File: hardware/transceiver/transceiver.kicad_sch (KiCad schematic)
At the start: 36 parts, among them J1 Conn_01x02, J2 Conn_01x04, J3 Micro_SD_Card_Det_Hirose_DM3AT, J4 Conn_Coaxial_Small, SW1 Reset, SW2 Boot, U1 SX1262IMLTRT, U2 PE4259, U4 ESP32-S3-MINI-1, Y1 32MHz

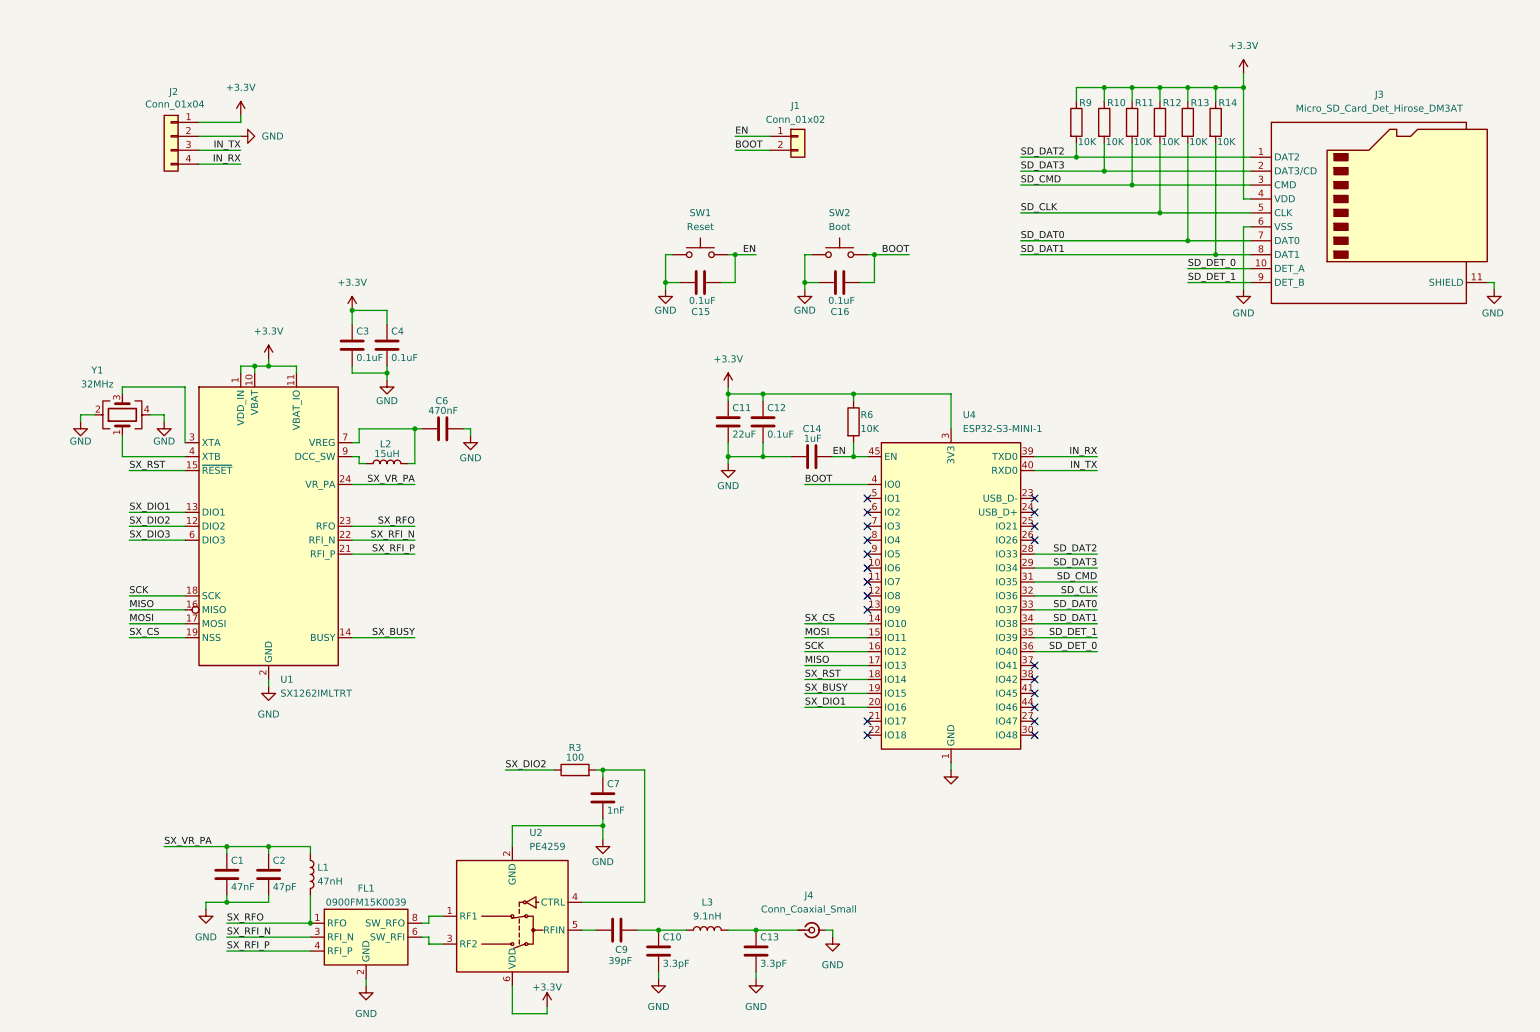
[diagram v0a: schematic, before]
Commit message: redesigned tranceiver
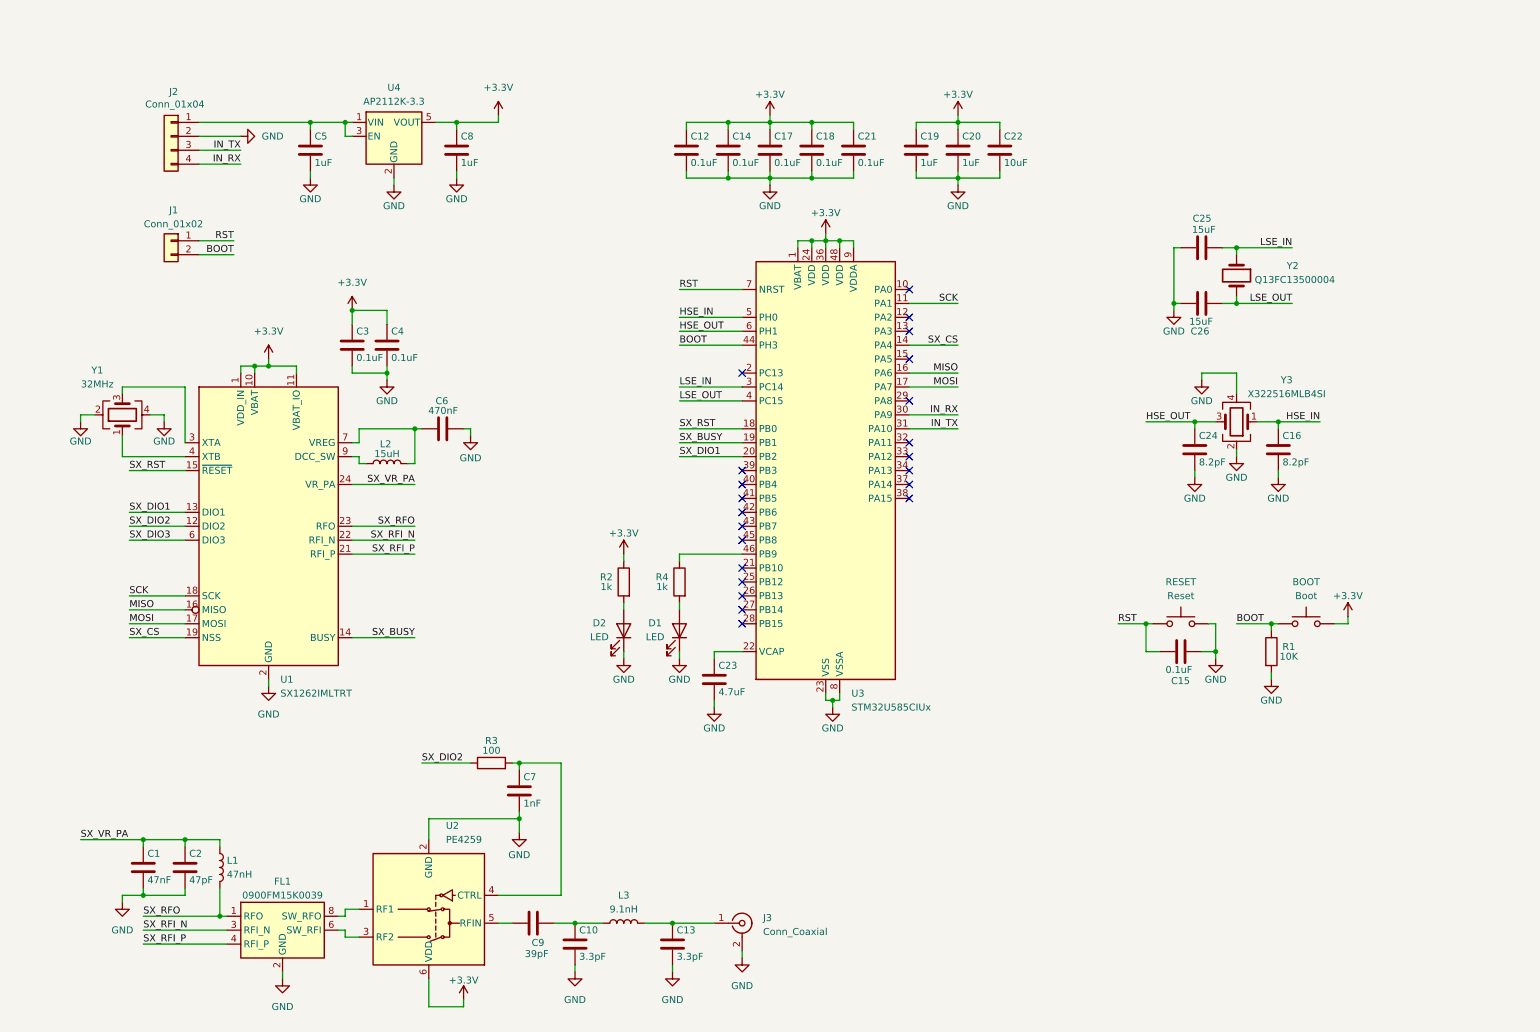
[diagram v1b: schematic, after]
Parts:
- removed C11: 22uF, Capacitor_SMD:C_0603_1608Metric, symbol Device:C
- removed J3: Micro_SD_Card_Det_Hirose_DM3AT, Connector_Card:microSD_HC_Hirose_DM3AT-SF-PEJM5, symbol Connector:Micro_SD_Card_Det_Hirose_DM3AT
- removed J4: Conn_Coaxial_Small, Connector_Coaxial:U.FL_Molex_MCRF_73412-0110_Vertical, symbol Connector:Conn_Coaxial_Small
- removed R10, R11, R12, R13, R14, R6, R9: 10K, Resistor_SMD:R_0402_1005Metric, symbol Device:R
- removed SW2: Boot, Button_Switch_SMD:SW_Push_SPST_NO_Alps_SKRK, symbol Switch:SW_Push
- removed U4: ESP32-S3-MINI-1, RF_Module:ESP32-S2-MINI-1, symbol RF_Module:ESP32-S3-MINI-1
- added BOOT: Boot, Button_Switch_SMD:SW_Push_SPST_NO_Alps_SKRK, symbol Switch:SW_Push
- added C17, C18, C21: 0.1uF, Capacitor_SMD:C_0402_1005Metric, symbol Device:C
- added C19, C20, C5, C8: 1uF, Capacitor_SMD:C_0603_1608Metric, symbol Device:C
- added C22: 10uF, Capacitor_SMD:C_0603_1608Metric, symbol Device:C
- added C23: 4.7uF, Capacitor_SMD:C_0402_1005Metric, symbol Device:C
- added C24: 8.2pF, Capacitor_SMD:C_0402_1005Metric, symbol Device:C
- added C25, C26: 15uF, Capacitor_SMD:C_0402_1005Metric, symbol Device:C
- added D1, D2: LED, LED_SMD:LED_0603_1608Metric, symbol Device:LED
- added J3: Conn_Coaxial, Connector_Coaxial:SMA_Amphenol_901-144_Vertical, symbol Connector:Conn_Coaxial
- added R1: 10K, Resistor_SMD:R_0402_1005Metric, symbol Device:R
- added R2, R4: 1k, Resistor_SMD:R_0402_1005Metric, symbol Device:R
- added U3: STM32U585CIUx, Package_DFN_QFN:QFN-48-1EP_7x7mm_P0.5mm_EP5.6x5.6mm, symbol MCU_ST_STM32U5:STM32U585CIUx
- added U4: AP2112K-3.3, Package_TO_SOT_SMD:SOT-23-5, symbol Regulator_Linear:AP2112K-3.3
- added Y2: Q13FC13500004, Crystal:Crystal_SMD_3215-2Pin_3.2x1.5mm, symbol Device:Crystal
- added Y3: X322516MLB4SI, Crystal:Crystal_SMD_3225-4Pin_3.2x2.5mm, symbol Device:Crystal_GND24
- C14: value 1uF -> 0.1uF
- C16: value 0.1uF -> 8.2pF
- renumbered SW1 to RESET
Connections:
- net +3.3V: now also C14.1, BOOT.1, C17.1, C18.1, C19.1, C20.1, C21.1, C22.1, C8.1, R2.1, U3.1 (VBAT), U3.24 (VDD), U3.36 (VDD), U3.48 (VDD), U3.9 (VDDA), U4.5 (VOUT); no longer J2.1 (Pin_1)
- net BOOT: now also BOOT.2, R1.1, U3.44 (PH3); no longer C16.2
- net GND: now also C14.2, C16.2, C17.2, C18.2, C19.2, C20.2, C21.2, C22.2, C23.2, C24.2, C25.1, C26.2, C5.2, C8.2, D1.1 (K), D2.1 (K), J3.2 (Ext), R1.2, U3.23 (VSS), U3.35 (VSS), U3.47 (VSS), U3.49 (VSS), U3.8 (VSSA), U4.2 (GND), Y3.2, Y3.4; no longer C14.1, C16.1
- net IN_RX: now also U3.30 (PA9)
- net IN_TX: now also U3.31 (PA10)
- net MISO: now also U3.16 (PA6)
- net MOSI: now also U3.17 (PA7)
- net SCK: now also U3.11 (PA1)
- net SX_BUSY: now also U3.19 (PB1)
- net SX_CS: now also U3.14 (PA4)
- net SX_DIO1: now also U3.20 (PB2)
- net SX_RST: now also U3.18 (PB0)
- net at C13.1, L3.2: now also J3.1 (In)
- net EN renamed RST
- net RST: now also U3.7 (NRST); no longer C14.2
- new net: C5.1, J2.1 (Pin_1), U4.1 (VIN), U4.3 (EN)
- new net: D2.2 (A), R2.2
- new net: D1.2 (A), R4.2
- new net: C23.1, U3.22 (VCAP)
- new net: R4.1, U3.46 (PB9)
- new net HSE_IN: C16.1, U3.5 (PH0), Y3.1
- new net HSE_OUT: C24.1, U3.6 (PH1), Y3.3
- new net LSE_IN: C25.2, U3.3 (PC14), Y2.1
- new net LSE_OUT: C26.1, U3.4 (PC15), Y2.2
- no-connect marks 21 -> 22
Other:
- moved on the sheet: C1, C10, C13, C15, C2, C7, C9, FL1, J1, L1, L3, R3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

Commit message: cleaning up transceiver
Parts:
- renumbered BOOT to BOOT1, C13 to C11, C23 to C13, C17 to C15, C18 to C16, C21 to C17, C19 to C18, C20 to C19, C22 to C20, C15 to C21, C24 to C22, C25 to C23, C26 to C24, C16 to C25, C5 to C3, C3 to C4, C4 to C5, C8 to C7, C7 to C8, D2 to D1, D1 to D2, J2 to J1, J1 to J2, R3 to R1, R4 to R3, R1 to R4, RESET to RESET1, U4 to U2, U2 to U3, U3 to U4

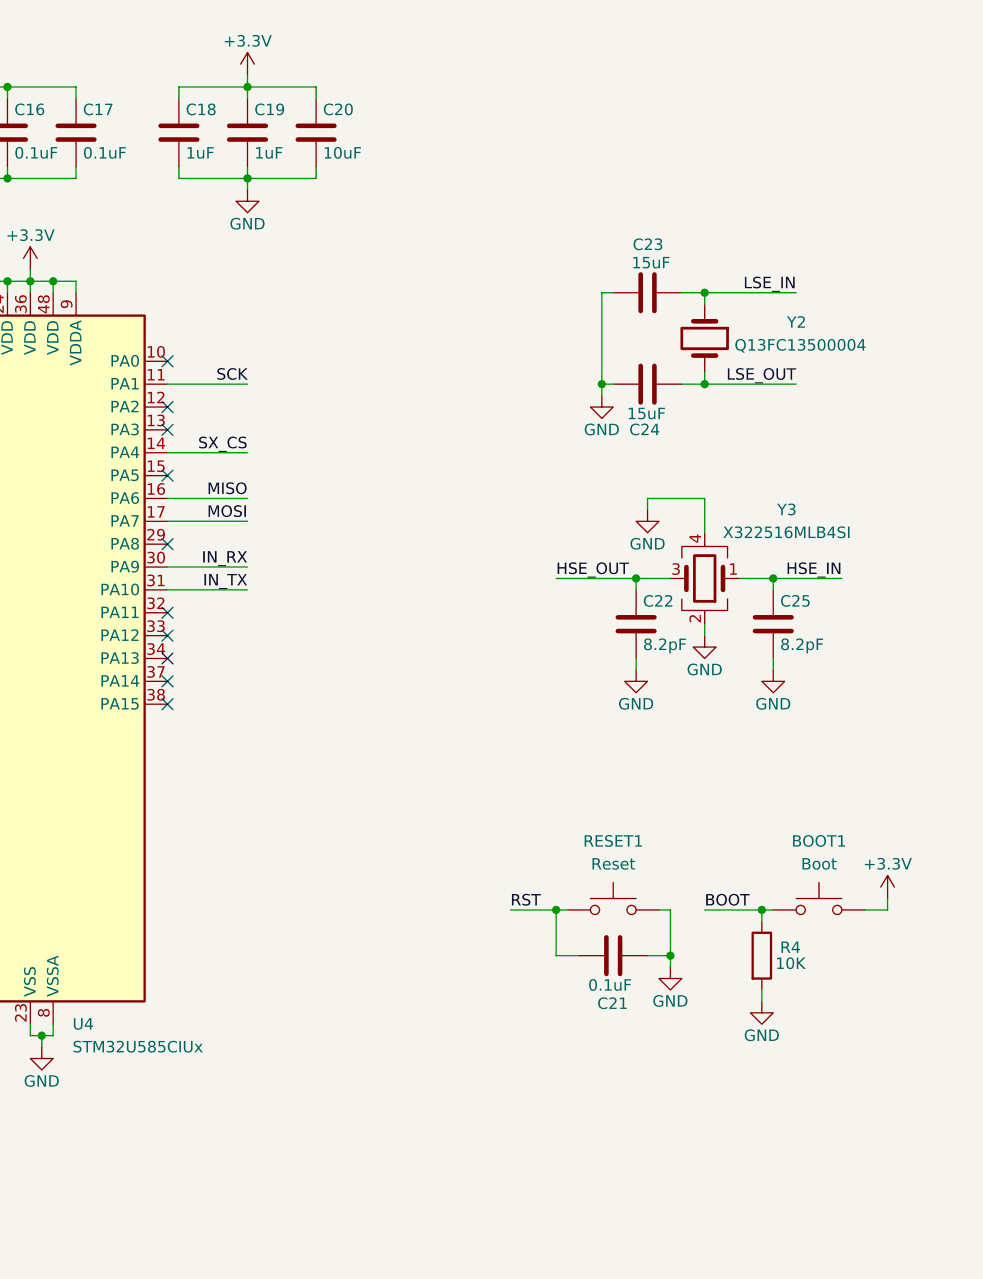
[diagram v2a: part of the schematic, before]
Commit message: added SWD to transceiver
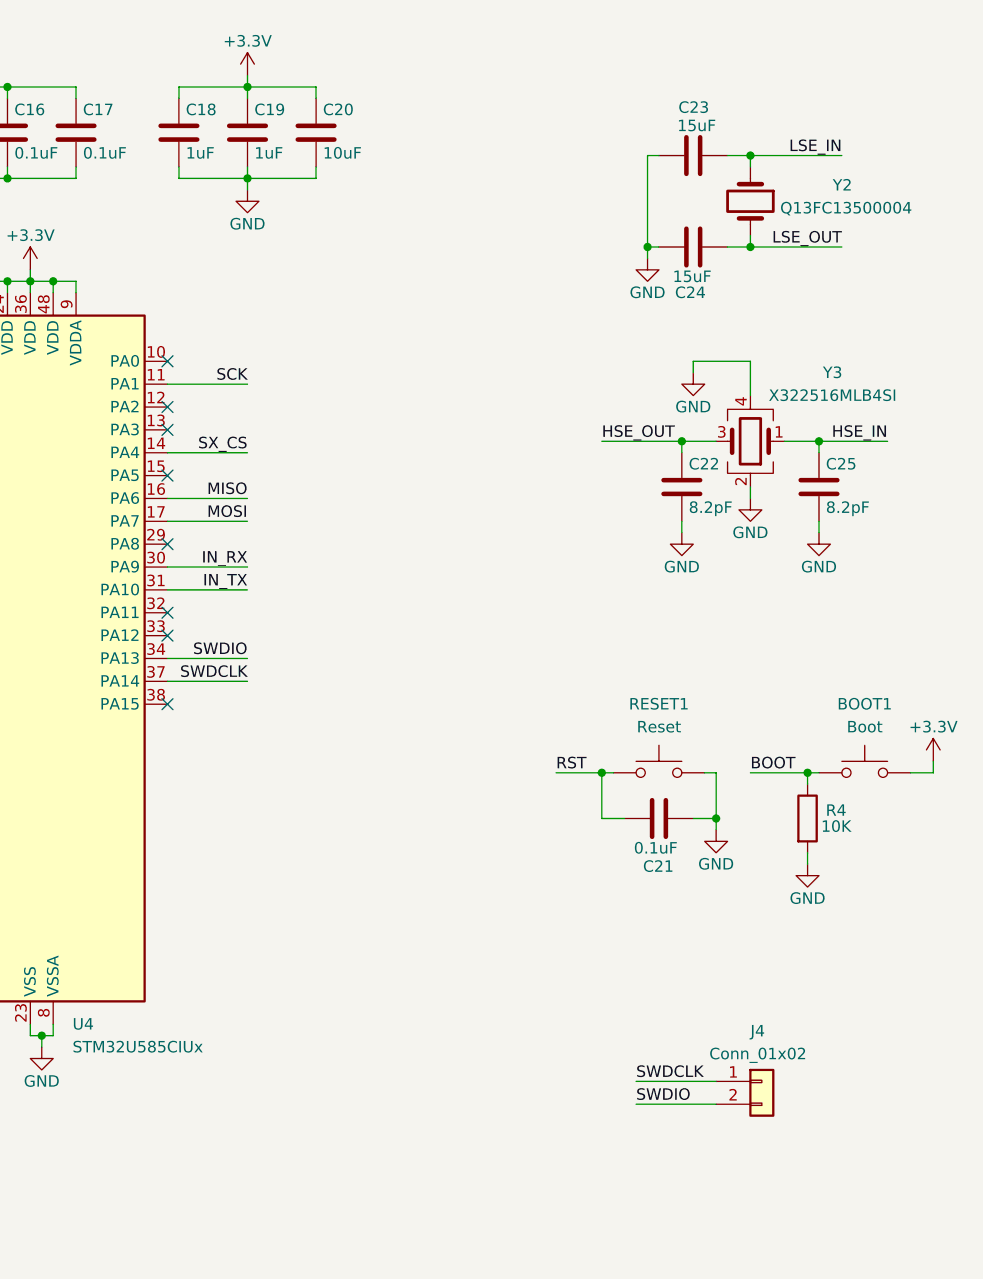
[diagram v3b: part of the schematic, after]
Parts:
- added J4: Conn_01x02, Connector_PinHeader_2.54mm:PinHeader_1x02_P2.54mm_Vertical, symbol Connector_Generic:Conn_01x02
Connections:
- net SWDIO: now reaches U4.34 (PA13)
- net SWDIO: now also J4.2 (Pin_2)
- net SWDCLK: now reaches U4.37 (PA14)
- net SWDCLK: now also J4.1 (Pin_1)
- no-connect marks 22 -> 20
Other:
- moved on the sheet: BOOT1, C21, C22, C23, C24, C25, R4, RESET1, Y2, Y3

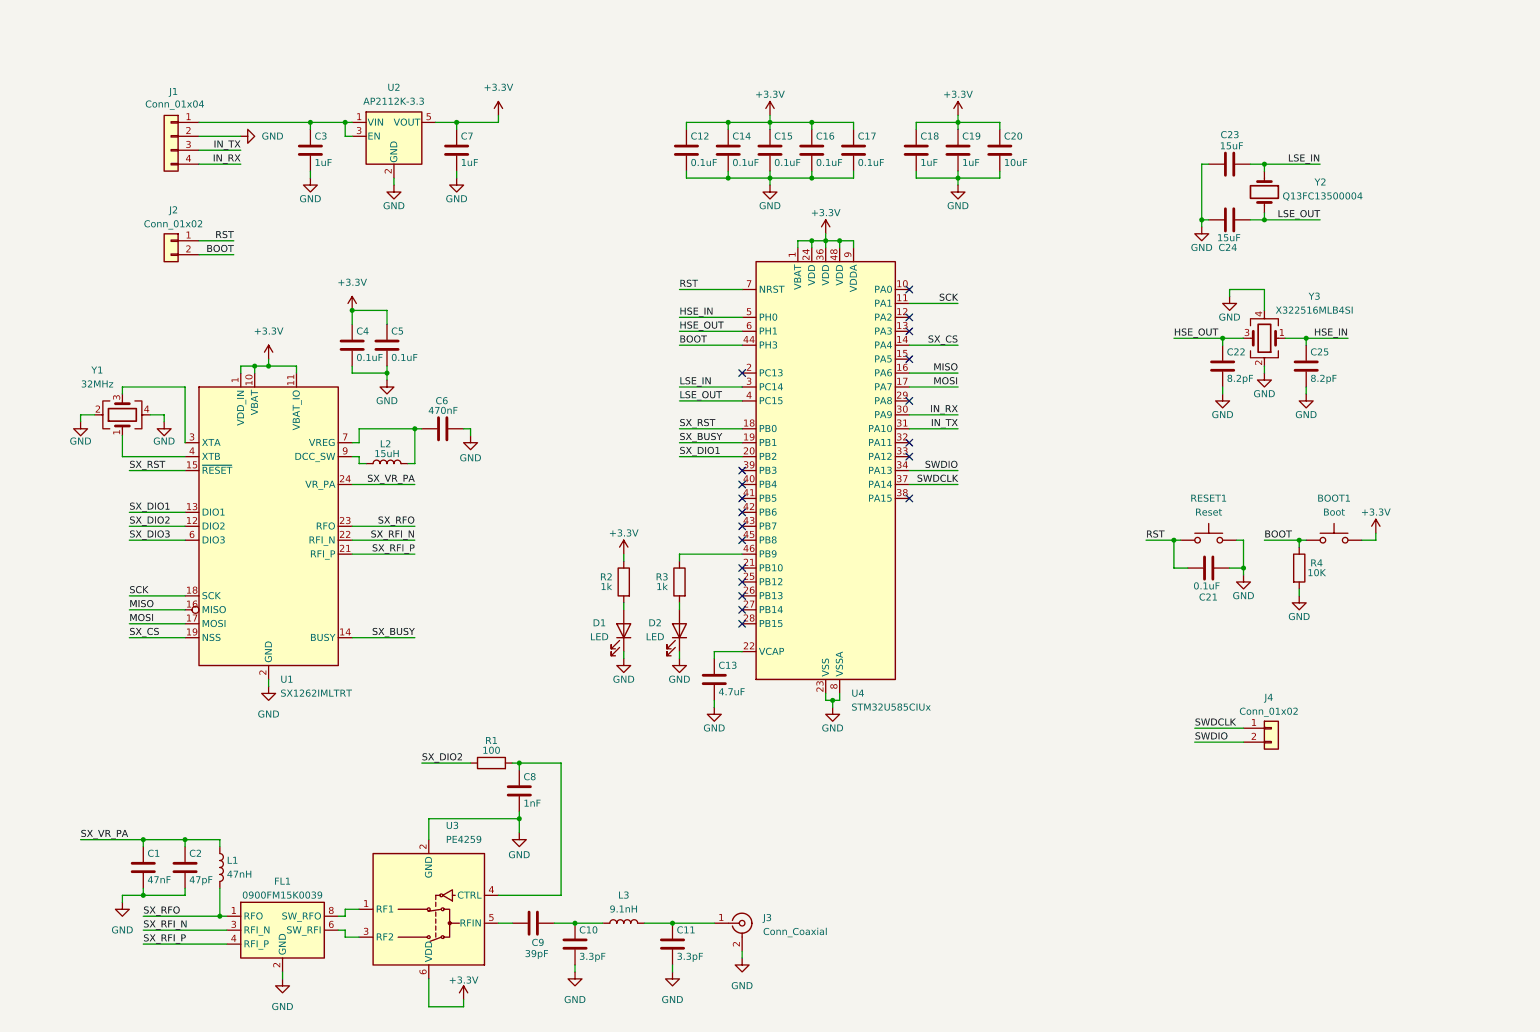
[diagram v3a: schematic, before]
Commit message: added lines to schematic
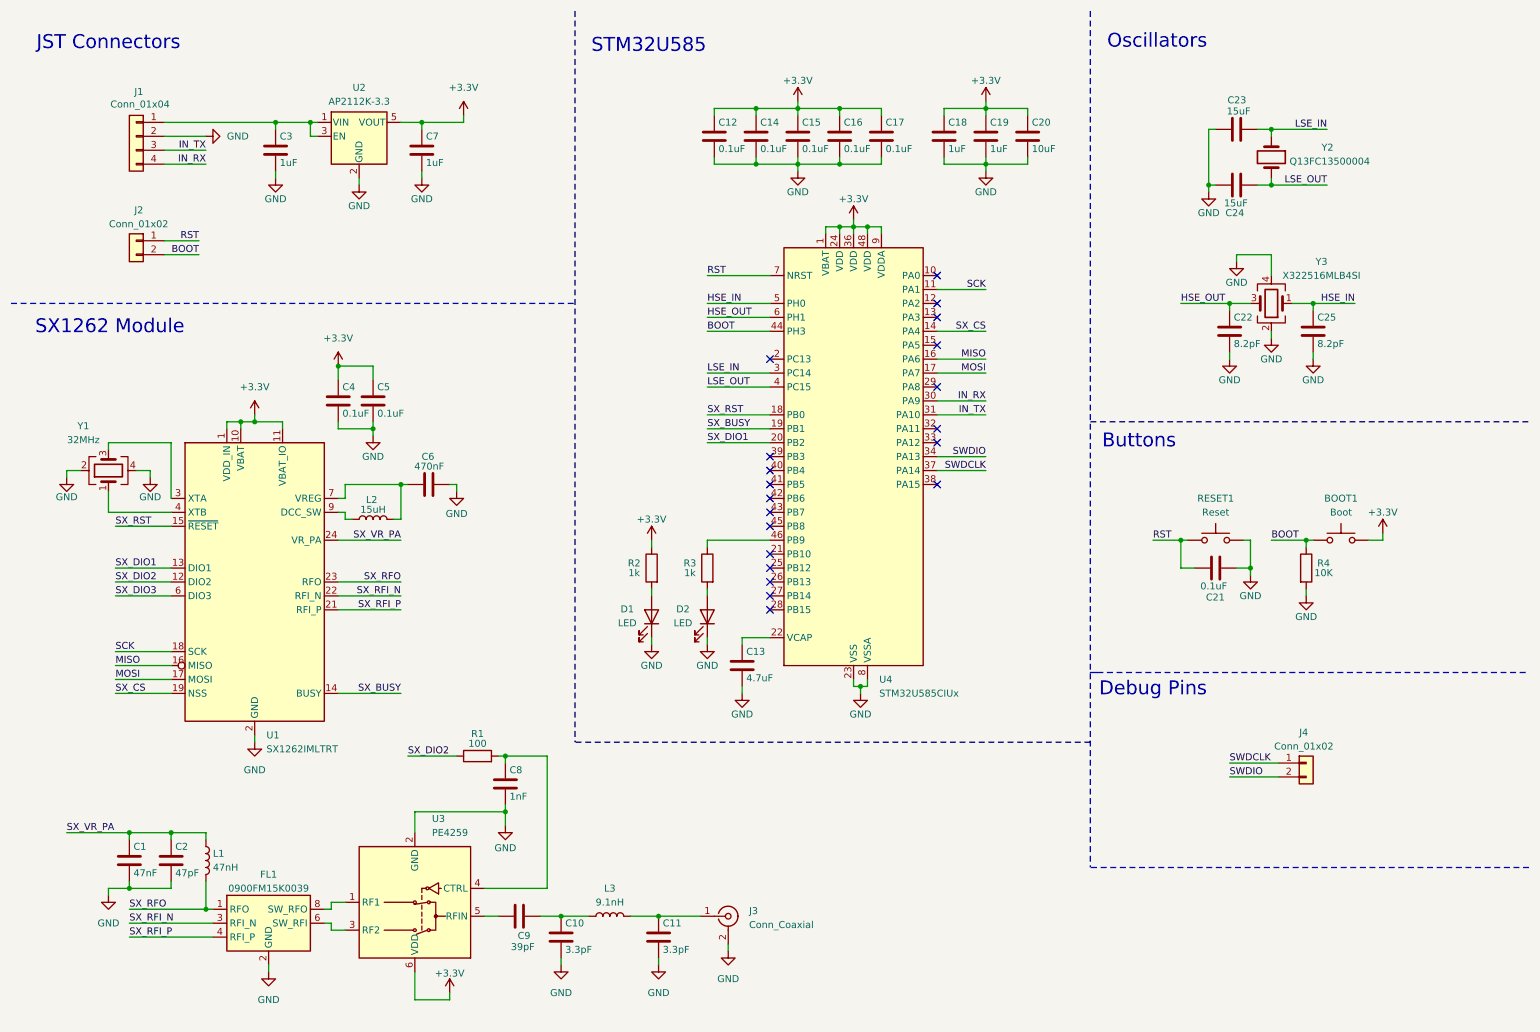
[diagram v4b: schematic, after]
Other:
- note added: "Buttons"
- note added: "Debug Pins"
- note added: "JST Connectors"
- note added: "Oscillators"
- note added: "STM32U585"
- note added: "SX1262 Module"
- moved on the sheet: BOOT1, C1, C10, C11, C12, C13, C14, C15, C16, C17, C18, C19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
